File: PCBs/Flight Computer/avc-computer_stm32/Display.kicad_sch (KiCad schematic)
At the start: 1 part, among them J6 OLED Display

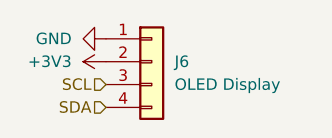
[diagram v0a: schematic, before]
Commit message: Began fixing reference designators
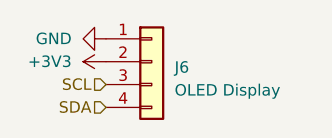
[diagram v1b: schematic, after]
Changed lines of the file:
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@@
   (symbol (lib_id "Connector_Generic:Conn_01x04") (at 165.1 90.17 0) (unit 1)
     (in_bom yes) (on_board yes) (dnp no) (fields_autoplaced)
-    (property "Reference" "J6" (at 167.64 90.1699 0)
+    (property "Reference" "J6" (at 167.64 90.805 0)
       (effects (font (size 1.27 1.27)) (justify left))
     )
-    (property "Value" "OLED Display" (at 167.64 92.7099 0)
+    (property "Value" "OLED Display" (at 167.64 93.345 0)
       (effects (font (size 1.27 1.27)) (justify left))
     )
@@
   (symbol (lib_id "power:+3V3") (at 160.02 90.17 90) (unit 1)
     (in_bom yes) (on_board yes) (dnp no) (fields_autoplaced)
-    (property "Reference" "#PWR0164" (at 163.83 90.17 0)
+    (property "Reference" "#PWR028" (at 163.83 90.17 0)
       (effects (font (size 1.27 1.27)) hide)
     )
@@
       (project "avc-computer"
         (path "/e63e39d7-6ac0-4ffd-8aa3-1841a4541b55/b9d51fc2-139c-4202-b21b-ffd40eaf3b64"
-          (reference "#PWR0164") (unit 1)
+          (reference "#PWR028") (unit 1)
         )
       )
@@
   (symbol (lib_id "power:GND") (at 160.02 87.63 270) (unit 1)
     (in_bom yes) (on_board yes) (dnp no) (fields_autoplaced)
-    (property "Reference" "#PWR0163" (at 153.67 87.63 0)
+    (property "Reference" "#PWR027" (at 153.67 87.63 0)
       (effects (font (size 1.27 1.27)) hide)
     )
@@
       (project "avc-computer"
         (path "/e63e39d7-6ac0-4ffd-8aa3-1841a4541b55/b9d51fc2-139c-4202-b21b-ffd40eaf3b64"
-          (reference "#PWR0163") (unit 1)
+          (reference "#PWR027") (unit 1)
         )
       )
